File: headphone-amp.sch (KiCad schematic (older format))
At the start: 21 parts, among them J1 AudioJack4, J2 AudioJack4, J3 Conn_01x02_Male, SW1 SW_SPDT, U1 RC4580, U2 TMA0512D

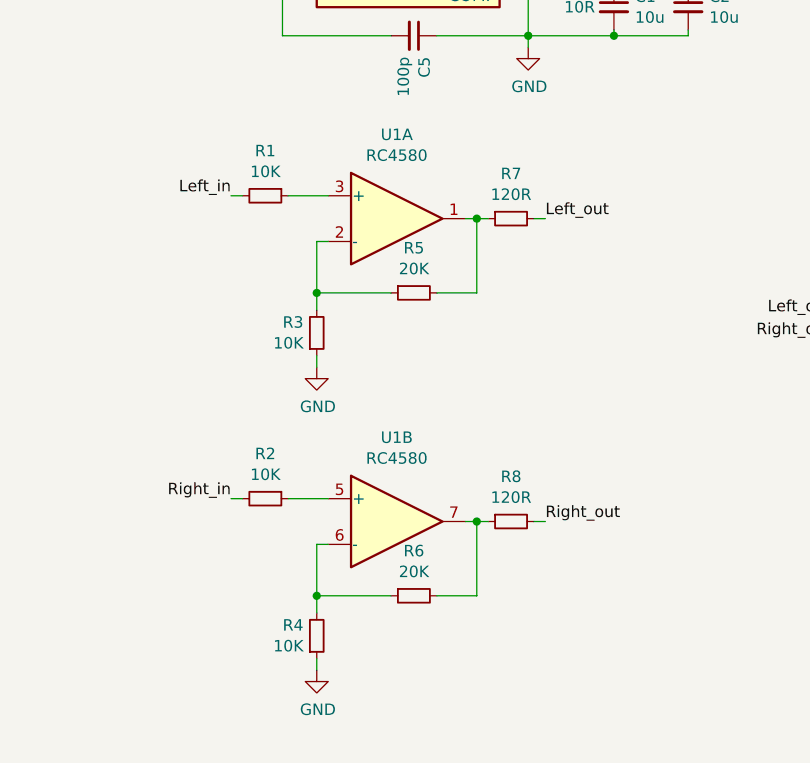
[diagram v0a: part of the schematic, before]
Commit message: changed feedback networks slightly
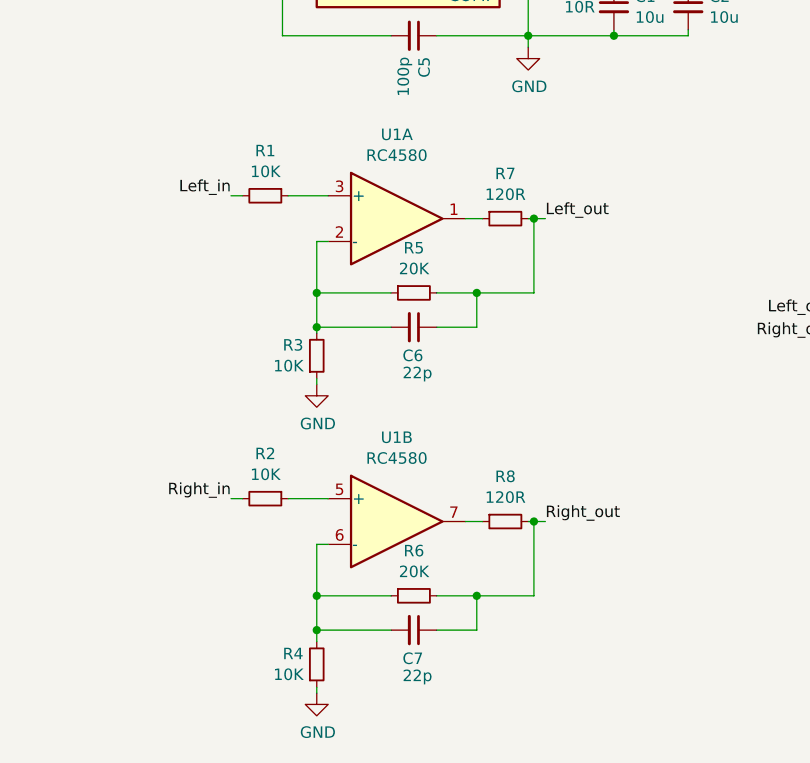
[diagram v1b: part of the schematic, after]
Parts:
- added C6, C7: 22p, Capacitor_SMD:C_0805_2012Metric, symbol Device:C_Small
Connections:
- net Left_out: now also R5.2, C6.1
- net Right_out: now also R6.2, C7.1
- net at R7.1, U1.1: no longer R5.2
- net at R3.2, R5.1, U1.2 (-): now also C6.2
- net at R4.2, R6.1, U1.6 (-): now also C7.2
- net at R8.1, U1.7: no longer R6.2
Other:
- moved on the sheet: R3, R4
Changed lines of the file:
@@
 L Device:R_Small R3
 U 1 1 5C5A5ADA
-P 3750 3775
-F 0 "R3" H 3692 3729 50  0000 R CNN
-F 1 "10K" H 3692 3820 50  0000 R CNN
-F 2 "Resistor_SMD:R_0805_2012Metric" H 3750 3775 50  0001 C CNN
-F 3 "~" H 3750 3775 50  0001 C CNN
-	1    3750 3775
+P 3750 3875
+F 0 "R3" H 3692 3829 50  0000 R CNN
+F 1 "10K" H 3692 3920 50  0000 R CNN
+F 2 "Resistor_SMD:R_0805_2012Metric" H 3750 3875 50  0001 C CNN
+F 3 "~" H 3750 3875 50  0001 C CNN
+	1    3750 3875
 	1    0    0    1
 $EndComp
@@
 Connection ~ 3750 3600
 Wire Wire Line
-	3750 3600 3750 3675
+	3750 3600 3750 3750
 Wire Wire Line
 	4275 3600 4450 3600
-Wire Wire Line
-	4450 3275 4400 3275
 Wire Wire Line
 	3625 3175 3800 3175
@@
 L power:GND #PWR0102
 U 1 1 5C5A651D
-P 3750 3925
-F 0 "#PWR0102" H 3750 3675 50  0001 C CNN
-F 1 "GND" H 3755 3752 50  0000 C CNN
-F 2 "" H 3750 3925 50  0001 C CNN
-F 3 "" H 3750 3925 50  0001 C CNN
-	1    3750 3925
-	1    0    0    -1
-$EndComp
-Wire Wire Line
-	3750 3925 3750 3875
+P 3750 4000
+F 0 "#PWR0102" H 3750 3750 50  0001 C CNN
+F 1 "GND" H 3755 3827 50  0000 C CNN
+F 2 "" H 3750 4000 50  0001 C CNN
+F 3 "" H 3750 4000 50  0001 C CNN
+	1    3750 4000
+	1    0    0    -1
+$EndComp
+Wire Wire Line
+	3750 4000 3750 3975
 Text Label 4750 3275 0    50   ~ 0
 Left_out
-$Comp
-L Device:R_Small R7
-U 1 1 5C5A66AA
-P 4600 3275
-F 0 "R7" V 4404 3275 50  0000 C CNN
-F 1 "120R" V 4495 3275 50  0000 C CNN
-F 2 "Resistor_SMD:R_0805_2012Metric" H 4600 3275 50  0001 C CNN
-F 3 "~" H 4600 3275 50  0001 C CNN
-	1    4600 3275
-	0    -1   1    0
-$EndComp
-Wire Wire Line
-	4450 3600 4450 3275
-Wire Wire Line
-	4500 3275 4450 3275
-Connection ~ 4450 3275
-Wire Wire Line
-	4750 3275 4700 3275
 $Comp
 L power:GND #PWR0103
@@
 L Device:R_Small R4
 U 1 1 5C5AADB1
-P 3750 5100
-F 0 "R4" H 3692 5054 50  0000 R CNN
-F 1 "10K" H 3692 5145 50  0000 R CNN
-F 2 "Resistor_SMD:R_0805_2012Metric" H 3750 5100 50  0001 C CNN
-F 3 "~" H 3750 5100 50  0001 C CNN
-	1    3750 5100
+P 3750 5225
+F 0 "R4" H 3692 5179 50  0000 R CNN
+F 1 "10K" H 3692 5270 50  0000 R CNN
+F 2 "Resistor_SMD:R_0805_2012Metric" H 3750 5225 50  0001 C CNN
+F 3 "~" H 3750 5225 50  0001 C CNN
+	1    3750 5225
 	1    0    0    1
 $EndComp
@@
 Connection ~ 3750 4925
 Wire Wire Line
-	3750 4925 3750 5000
+	3750 4925 3750 5075
 Wire Wire Line
 	4275 4925 4450 4925
-Wire Wire Line
-	4450 4600 4400 4600
 Wire Wire Line
 	3625 4500 3800 4500
@@
 L power:GND #PWR0108
 U 1 1 5C5AADC9
-P 3750 5250
-F 0 "#PWR0108" H 3750 5000 50  0001 C CNN
-F 1 "GND" H 3755 5077 50  0000 C CNN
-F 2 "" H 3750 5250 50  0001 C CNN
-F 3 "" H 3750 5250 50  0001 C CNN
-	1    3750 5250
-	1    0    0    -1
-$EndComp
-Wire Wire Line
-	3750 5250 3750 5200
+P 3750 5350
+F 0 "#PWR0108" H 3750 5100 50  0001 C CNN
+F 1 "GND" H 3755 5177 50  0000 C CNN
+F 2 "" H 3750 5350 50  0001 C CNN
+F 3 "" H 3750 5350 50  0001 C CNN
+	1    3750 5350
+	1    0    0    -1
+$EndComp
+Wire Wire Line
+	3750 5350 3750 5325
 Text Label 4750 4600 0    50   ~ 0
 Right_out
-$Comp
-L Device:R_Small R8
-U 1 1 5C5AADD1
-P 4600 4600
-F 0 "R8" V 4404 4600 50  0000 C CNN
-F 1 "120R" V 4495 4600 50  0000 C CNN
-F 2 "Resistor_SMD:R_0805_2012Metric" H 4600 4600 50  0001 C CNN
-F 3 "~" H 4600 4600 50  0001 C CNN
-	1    4600 4600
-	0    -1   1    0
-$EndComp
-Wire Wire Line
-	4450 4925 4450 4600
-Wire Wire Line
-	4500 4600 4450 4600
-Connection ~ 4450 4600
-Wire Wire Line
-	4750 4600 4700 4600
 $Comp
 L Connector:AudioJack4 J2
@@
 Wire Wire Line
 	3600 2250 3650 2250
+$Comp
+L Device:C_Small C6
+U 1 1 5C5B31D4
+P 4175 3750
+F 0 "C6" V 4300 3700 50  0000 L CNN
+F 1 "22p" V 4375 3700 50  0000 L CNN
+F 2 "Capacitor_SMD:C_0805_2012Metric" H 4175 3750 50  0001 C CNN
+F 3 "~" H 4175 3750 50  0001 C CNN
+	1    4175 3750
+	0    1    1    0
+$EndComp
+Wire Wire Line
+	4075 3750 3750 3750
+Connection ~ 3750 3750
+Wire Wire Line
+	3750 3750 3750 3775
+Wire Wire Line
+	4275 3750 4450 3750
+Wire Wire Line
+	4450 3750 4450 3600
+$Comp
+L Device:C_Small C7
+U 1 1 5C5B7CE8
+P 4175 5075
+F 0 "C7" V 4300 5025 50  0000 L CNN
+F 1 "22p" V 4375 5025 50  0000 L CNN
+F 2 "Capacitor_SMD:C_0805_2012Metric" H 4175 5075 50  0001 C CNN
+F 3 "~" H 4175 5075 50  0001 C CNN
+	1    4175 5075
+	0    1    1    0
+$EndComp
+Wire Wire Line
+	4075 5075 3750 5075
+Connection ~ 3750 5075
+Wire Wire Line
+	3750 5075 3750 5125
+Wire Wire Line
+	4275 5075 4450 5075
+Wire Wire Line
+	4450 5075 4450 4925
+$Comp
+L Device:R_Small R7
+U 1 1 5C5BFFE4
+P 4575 3275
+F 0 "R7" V 4379 3275 50  0000 C CNN
+F 1 "120R" V 4470 3275 50  0000 C CNN
+F 2 "Resistor_SMD:R_0805_2012Metric" H 4575 3275 50  0001 C CNN
+F 3 "~" H 4575 3275 50  0001 C CNN
+	1    4575 3275
+	0    -1   1    0
+$EndComp
+Wire Wire Line
+	4475 3275 4400 3275
+Wire Wire Line
+	4675 3275 4700 3275
+Wire Wire Line
+	4450 3600 4700 3600
+Wire Wire Line
+	4700 3600 4700 3275
+Connection ~ 4450 3600
+Connection ~ 4700 3275
+Wire Wire Line
+	4700 3275 4750 3275
+$Comp
+L Device:R_Small R8
+U 1 1 5C5C459C
+P 4575 4600
+F 0 "R8" V 4379 4600 50  0000 C CNN
+F 1 "120R" V 4470 4600 50  0000 C CNN
+F 2 "Resistor_SMD:R_0805_2012Metric" H 4575 4600 50  0001 C CNN
+F 3 "~" H 4575 4600 50  0001 C CNN
+	1    4575 4600
+	0    -1   1    0
+$EndComp
+Wire Wire Line
+	4475 4600 4400 4600
+Wire Wire Line
+	4675 4600 4700 4600
+Wire Wire Line
+	4700 4600 4700 4925
+Wire Wire Line
+	4700 4925 4450 4925
+Connection ~ 4700 4600
+Wire Wire Line
+	4700 4600 4750 4600
+Connection ~ 4450 4925
 $EndSCHEMATC

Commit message: tag for prototype production
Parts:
- U2: symbol custom:TMAxxxxD -> headphone-amp-rescue:TMAxxxxD-custom
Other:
- moved on the sheet: J1, J2
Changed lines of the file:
@@
 $EndDescr
 $Comp
-L custom:TMAxxxxD U2
+L headphone-amp-rescue:TMAxxxxD-custom U2
 U 1 1 5C5A5764
 P 4150 2350
@@
 L Connector:AudioJack4 J1
 U 1 1 5C5A5EA8
-P 1825 3550
-F 0 "J1" H 1495 3433 50  0000 R CNN
-F 1 "AudioJack4" H 1495 3524 50  0000 R CNN
-F 2 "Connector_Audio:Jack_3.5mm_PJ320D_Horizontal" H 1825 3550 50  0001 C CNN
-F 3 "~" H 1825 3550 50  0001 C CNN
-	1    1825 3550
+P 2100 3850
+F 0 "J1" H 1770 3733 50  0000 R CNN
+F 1 "AudioJack4" H 1770 3824 50  0000 R CNN
+F 2 "Connector_Audio:Jack_3.5mm_PJ320D_Horizontal" H 2100 3850 50  0001 C CNN
+F 3 "~" H 2100 3850 50  0001 C CNN
+	1    2100 3850
 	1    0    0    1
 $EndComp
@@
 L power:GND #PWR0101
 U 1 1 5C5A5F4D
-P 2075 3700
-F 0 "#PWR0101" H 2075 3450 50  0001 C CNN
-F 1 "GND" H 2080 3527 50  0000 C CNN
-F 2 "" H 2075 3700 50  0001 C CNN
-F 3 "" H 2075 3700 50  0001 C CNN
-	1    2075 3700
-	1    0    0    -1
-$EndComp
-Wire Wire Line
-	2075 3700 2075 3650
-Wire Wire Line
-	2075 3650 2025 3650
-Text Label 2075 3350 0    50   ~ 0
+P 2350 4000
+F 0 "#PWR0101" H 2350 3750 50  0001 C CNN
+F 1 "GND" H 2355 3827 50  0000 C CNN
+F 2 "" H 2350 4000 50  0001 C CNN
+F 3 "" H 2350 4000 50  0001 C CNN
+	1    2350 4000
+	1    0    0    -1
+$EndComp
+Wire Wire Line
+	2350 4000 2350 3950
+Wire Wire Line
+	2350 3950 2300 3950
+Text Label 2350 3650 0    50   ~ 0
 Left_in
-Text Label 2075 3450 0    50   ~ 0
+Text Label 2350 3750 0    50   ~ 0
 Right_in
 Wire Wire Line
-	2075 3350 2025 3350
-Wire Wire Line
-	2025 3450 2075 3450
+	2350 3650 2300 3650
+Wire Wire Line
+	2300 3750 2350 3750
 Text Label 3375 3175 2    50   ~ 0
 Left_in
@@
 L Connector:AudioJack4 J2
 U 1 1 5C5AB90E
-P 6250 3900
-F 0 "J2" H 5920 3783 50  0000 R CNN
-F 1 "AudioJack4" H 5920 3874 50  0000 R CNN
-F 2 "Connector_Audio:Jack_3.5mm_PJ320D_Horizontal" H 6250 3900 50  0001 C CNN
-F 3 "~" H 6250 3900 50  0001 C CNN
-	1    6250 3900
+P 6075 3875
+F 0 "J2" H 5745 3758 50  0000 R CNN
+F 1 "AudioJack4" H 5745 3849 50  0000 R CNN
+F 2 "Connector_Audio:Jack_3.5mm_PJ320D_Horizontal" H 6075 3875 50  0001 C CNN
+F 3 "~" H 6075 3875 50  0001 C CNN
+	1    6075 3875
 	-1   0    0    1
 $EndComp
@@
 L power:GND #PWR0109
 U 1 1 5C5AB915
-P 6000 4050
-F 0 "#PWR0109" H 6000 3800 50  0001 C CNN
-F 1 "GND" H 6005 3877 50  0000 C CNN
-F 2 "" H 6000 4050 50  0001 C CNN
-F 3 "" H 6000 4050 50  0001 C CNN
-	1    6000 4050
+P 5825 4025
+F 0 "#PWR0109" H 5825 3775 50  0001 C CNN
+F 1 "GND" H 5830 3852 50  0000 C CNN
+F 2 "" H 5825 4025 50  0001 C CNN
+F 3 "" H 5825 4025 50  0001 C CNN
+	1    5825 4025
 	-1   0    0    -1
 $EndComp
 Wire Wire Line
-	6000 4050 6000 4000
-Wire Wire Line
-	6000 4000 6050 4000
-Text Label 6000 3700 2    50   ~ 0
+	5825 4025 5825 3975
+Wire Wire Line
+	5825 3975 5875 3975
+Text Label 5825 3675 2    50   ~ 0
 Left_out
-Text Label 6000 3800 2    50   ~ 0
+Text Label 5825 3775 2    50   ~ 0
 Right_out
 Wire Wire Line
-	6000 3700 6050 3700
-Wire Wire Line
-	6050 3800 6000 3800
+	5825 3675 5875 3675
+Wire Wire Line
+	5875 3775 5825 3775
 $Comp
 L Connector:Conn_01x02_Male J3

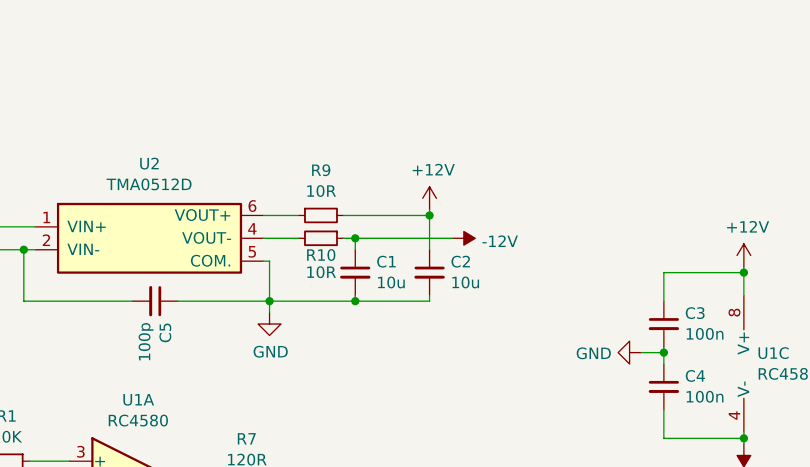
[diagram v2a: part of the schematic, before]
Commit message: changed filtering network
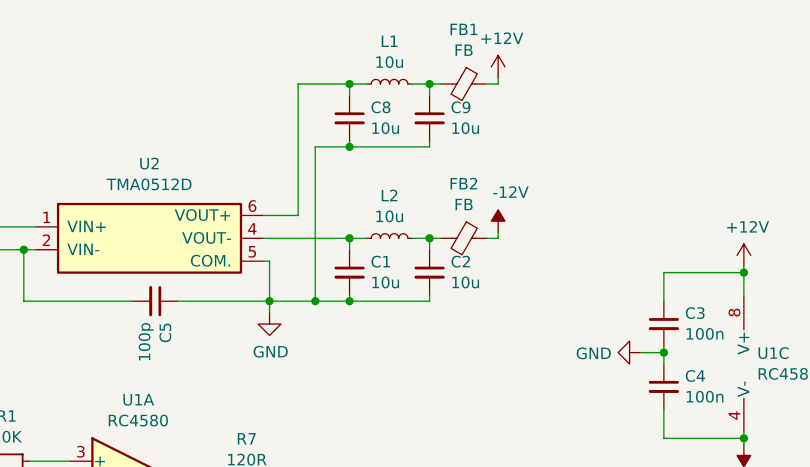
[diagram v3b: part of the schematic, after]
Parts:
- removed R10, R9: 10R, Resistor_SMD:R_0805_2012Metric, symbol Device:R_Small
- added C8, C9: 10u, Capacitor_SMD:C_0805_2012Metric, symbol Device:C_Small
- added FB1, FB2: FB, Inductor_SMD:L_0805_2012Metric, symbol Device:Ferrite_Bead_Small
- added L1, L2: 10u, Inductor_SMD:L_0805_2012Metric, symbol Device:L_Small
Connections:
- net +12V: now also FB1.1; no longer C2.1
- net -12V: now also FB2.1; no longer C1.1
- net GND: now also C8.2, C9.2
- net at U2.4 (VOUT-): now also C1.1, L2.1
- net at U2.6 (VOUT+): now also C8.1, L1.1
- new net: C2.1, FB2.2, L2.2
- new net: C9.1, FB1.2, L1.2
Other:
- moved on the sheet: C1
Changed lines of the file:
@@
 L power:+12V #PWR0106
 U 1 1 5C5A736C
-P 5375 2075
-F 0 "#PWR0106" H 5375 1925 50  0001 C CNN
-F 1 "+12V" H 5390 2248 50  0000 C CNN
-F 2 "" H 5375 2075 50  0001 C CNN
-F 3 "" H 5375 2075 50  0001 C CNN
-	1    5375 2075
+P 5675 1500
+F 0 "#PWR0106" H 5675 1350 50  0001 C CNN
+F 1 "+12V" H 5690 1673 50  0000 C CNN
+F 2 "" H 5675 1500 50  0001 C CNN
+F 3 "" H 5675 1500 50  0001 C CNN
+	1    5675 1500
 	1    0    0    -1
 $EndComp
@@
 L power:-12V #PWR0107
 U 1 1 5C5A73B8
-P 5475 2200
-F 0 "#PWR0107" H 5475 2300 50  0001 C CNN
-F 1 "-12V" V 5490 2328 50  0000 L CNN
-F 2 "" H 5475 2200 50  0001 C CNN
-F 3 "" H 5475 2200 50  0001 C CNN
-	1    5475 2200
-	0    1    1    0
-$EndComp
-$Comp
-L Device:R_Small R9
-U 1 1 5C5A74AA
-P 4900 2100
-F 0 "R9" V 4704 2100 50  0000 C CNN
-F 1 "10R" V 4795 2100 50  0000 C CNN
-F 2 "Resistor_SMD:R_0805_2012Metric" H 4900 2100 50  0001 C CNN
-F 3 "~" H 4900 2100 50  0001 C CNN
-	1    4900 2100
-	0    -1   1    0
-$EndComp
-$Comp
-L Device:R_Small R10
-U 1 1 5C5A7777
-P 4900 2200
-F 0 "R10" V 4975 2200 50  0000 C CNN
-F 1 "10R" V 5050 2200 50  0000 C CNN
-F 2 "Resistor_SMD:R_0805_2012Metric" H 4900 2200 50  0001 C CNN
-F 3 "~" H 4900 2200 50  0001 C CNN
-	1    4900 2200
-	0    1    1    0
-$EndComp
-Wire Wire Line
-	4800 2200 4650 2200
+P 5675 2175
+F 0 "#PWR0107" H 5675 2275 50  0001 C CNN
+F 1 "-12V" H 5650 2350 50  0000 L CNN
+F 2 "" H 5675 2175 50  0001 C CNN
+F 3 "" H 5675 2175 50  0001 C CNN
+	1    5675 2175
+	1    0    0    -1
+$EndComp
 Wire Wire Line
 	4800 2100 4650 2100
@@
 L Device:C_Small C1
 U 1 1 5C5A8D97
-P 5050 2350
-F 0 "C1" H 5142 2396 50  0000 L CNN
-F 1 "10u" H 5142 2305 50  0000 L CNN
-F 2 "Capacitor_SMD:C_0805_2012Metric" H 5050 2350 50  0001 C CNN
-F 3 "~" H 5050 2350 50  0001 C CNN
-	1    5050 2350
+P 5025 2350
+F 0 "C1" H 5117 2396 50  0000 L CNN
+F 1 "10u" H 5117 2305 50  0000 L CNN
+F 2 "Capacitor_SMD:C_0805_2012Metric" H 5025 2350 50  0001 C CNN
+F 3 "~" H 5025 2350 50  0001 C CNN
+	1    5025 2350
 	1    0    0    -1
 $EndComp
@@
 	1    0    0    -1
 $EndComp
-Wire Wire Line
-	5375 2250 5375 2100
-Wire Wire Line
-	5375 2100 5000 2100
-Wire Wire Line
-	5000 2200 5050 2200
-Wire Wire Line
-	5050 2200 5050 2250
-Wire Wire Line
-	5375 2450 5375 2475
-Wire Wire Line
-	5375 2475 5050 2475
 Connection ~ 4675 2475
 Wire Wire Line
 	4675 2475 4675 2300
-Wire Wire Line
-	5050 2450 5050 2475
-Connection ~ 5050 2475
-Wire Wire Line
-	5050 2475 4675 2475
-Wire Wire Line
-	5375 2075 5375 2100
-Connection ~ 5375 2100
-Wire Wire Line
-	5475 2200 5050 2200
-Connection ~ 5050 2200
 $Comp
 L Amplifier_Operational:RC4580 U1
@@
 	4700 4600 4750 4600
 Connection ~ 4450 4925
+$Comp
+L Device:L_Small L2
+U 1 1 5C5CCE1A
+P 5200 2200
+F 0 "L2" V 5385 2200 50  0000 C CNN
+F 1 "10u" V 5294 2200 50  0000 C CNN
+F 2 "Inductor_SMD:L_0805_2012Metric" H 5200 2200 50  0001 C CNN
+F 3 "~" H 5200 2200 50  0001 C CNN
+	1    5200 2200
+	0    -1   -1   0
+$EndComp
+Wire Wire Line
+	4650 2200 5025 2200
+Wire Wire Line
+	5025 2250 5025 2200
+Connection ~ 5025 2200
+Wire Wire Line
+	5025 2200 5100 2200
+Wire Wire Line
+	5375 2250 5375 2200
+Wire Wire Line
+	5375 2200 5300 2200
+Wire Wire Line
+	5025 2450 5025 2475
+Connection ~ 5025 2475
+Wire Wire Line
+	5025 2475 5375 2475
+Wire Wire Line
+	5375 2450 5375 2475
+$Comp
+L Device:C_Small C8
+U 1 1 5C5D3976
+P 5025 1675
+F 0 "C8" H 5117 1721 50  0000 L CNN
+F 1 "10u" H 5117 1630 50  0000 L CNN
+F 2 "Capacitor_SMD:C_0805_2012Metric" H 5025 1675 50  0001 C CNN
+F 3 "~" H 5025 1675 50  0001 C CNN
+	1    5025 1675
+	1    0    0    -1
+$EndComp
+$Comp
+L Device:C_Small C9
+U 1 1 5C5D397D
+P 5375 1675
+F 0 "C9" H 5467 1721 50  0000 L CNN
+F 1 "10u" H 5467 1630 50  0000 L CNN
+F 2 "Capacitor_SMD:C_0805_2012Metric" H 5375 1675 50  0001 C CNN
+F 3 "~" H 5375 1675 50  0001 C CNN
+	1    5375 1675
+	1    0    0    -1
+$EndComp
+$Comp
+L Device:L_Small L1
+U 1 1 5C5D3985
+P 5200 1525
+F 0 "L1" V 5385 1525 50  0000 C CNN
+F 1 "10u" V 5294 1525 50  0000 C CNN
+F 2 "Inductor_SMD:L_0805_2012Metric" H 5200 1525 50  0001 C CNN
+F 3 "~" H 5200 1525 50  0001 C CNN
+	1    5200 1525
+	0    -1   -1   0
+$EndComp
+Wire Wire Line
+	5025 1575 5025 1525
+Wire Wire Line
+	5025 1525 5100 1525
+Wire Wire Line
+	5375 1575 5375 1525
+Wire Wire Line
+	5375 1525 5300 1525
+Wire Wire Line
+	5025 1775 5025 1800
+Wire Wire Line
+	5025 1800 5375 1800
+Wire Wire Line
+	5375 1775 5375 1800
+Wire Wire Line
+	5025 1525 4800 1525
+Connection ~ 5025 1525
+Wire Wire Line
+	5025 1800 4875 1800
+Connection ~ 5025 1800
+Wire Wire Line
+	4675 2475 4875 2475
+Wire Wire Line
+	4875 1800 4875 2475
+Connection ~ 4875 2475
+Wire Wire Line
+	4875 2475 5025 2475
+Wire Wire Line
+	4800 1525 4800 2100
+$Comp
+L Device:Ferrite_Bead_Small FB1
+U 1 1 5C5E62E2
+P 5525 1525
+F 0 "FB1" V 5288 1525 50  0000 C CNN
+F 1 "FB" V 5379 1525 50  0000 C CNN
+F 2 "Inductor_SMD:L_0805_2012Metric" V 5455 1525 50  0001 C CNN
+F 3 "~" H 5525 1525 50  0001 C CNN
+	1    5525 1525
+	0    1    1    0
+$EndComp
+$Comp
+L Device:Ferrite_Bead_Small FB2
+U 1 1 5C5E6593
+P 5525 2200
+F 0 "FB2" V 5288 2200 50  0000 C CNN
+F 1 "FB" V 5379 2200 50  0000 C CNN
+F 2 "Inductor_SMD:L_0805_2012Metric" V 5455 2200 50  0001 C CNN
+F 3 "~" H 5525 2200 50  0001 C CNN
+	1    5525 2200
+	0    1    1    0
+$EndComp
+Wire Wire Line
+	5425 2200 5375 2200
+Connection ~ 5375 2200
+Wire Wire Line
+	5375 1525 5425 1525
+Connection ~ 5375 1525
+Wire Wire Line
+	5675 1500 5675 1525
+Wire Wire Line
+	5675 1525 5625 1525
+Wire Wire Line
+	5675 2175 5675 2200
+Wire Wire Line
+	5675 2200 5625 2200
 $EndSCHEMATC

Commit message: minor changes to filtering networks
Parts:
- C2, C9: value 10u -> 20u
- C5: value 100p -> 12n
- C6, C7: value 22p -> 402p
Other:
- note added: "20u = 2x stacked 10u"
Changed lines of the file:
@@
 P 5375 2350
 F 0 "C2" H 5467 2396 50  0000 L CNN
-F 1 "10u" H 5467 2305 50  0000 L CNN
+F 1 "20u" H 5467 2305 50  0000 L CNN
 F 2 "Capacitor_SMD:C_0805_2012Metric" H 5375 2350 50  0001 C CNN
 F 3 "~" H 5375 2350 50  0001 C CNN
@@
 P 4175 2475
 F 0 "C5" H 4267 2521 50  0000 L CNN
-F 1 "100p" H 4267 2430 50  0000 L CNN
+F 1 "12n" H 4267 2430 50  0000 L CNN
 F 2 "Capacitor_SMD:C_0805_2012Metric" H 4175 2475 50  0001 C CNN
 F 3 "~" H 4175 2475 50  0001 C CNN
@@
 P 4175 3750
 F 0 "C6" V 4300 3700 50  0000 L CNN
-F 1 "22p" V 4375 3700 50  0000 L CNN
+F 1 "402p" V 4375 3700 50  0000 L CNN
 F 2 "Capacitor_SMD:C_0805_2012Metric" H 4175 3750 50  0001 C CNN
 F 3 "~" H 4175 3750 50  0001 C CNN
@@
 P 4175 5075
 F 0 "C7" V 4300 5025 50  0000 L CNN
-F 1 "22p" V 4375 5025 50  0000 L CNN
+F 1 "402p" V 4375 5025 50  0000 L CNN
 F 2 "Capacitor_SMD:C_0805_2012Metric" H 4175 5075 50  0001 C CNN
 F 3 "~" H 4175 5075 50  0001 C CNN
@@
 P 5375 1675
 F 0 "C9" H 5467 1721 50  0000 L CNN
-F 1 "10u" H 5467 1630 50  0000 L CNN
+F 1 "20u" H 5467 1630 50  0000 L CNN
 F 2 "Capacitor_SMD:C_0805_2012Metric" H 5375 1675 50  0001 C CNN
 F 3 "~" H 5375 1675 50  0001 C CNN
@@
 Wire Wire Line
 	5675 2200 5625 2200
+Text Notes 5050 2600 0    50   ~ 0
+20u = 2x stacked 10u
 $EndSCHEMATC
